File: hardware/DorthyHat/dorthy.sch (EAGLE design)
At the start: 40 parts, among them J1 90325-0004, J2 90325-0004

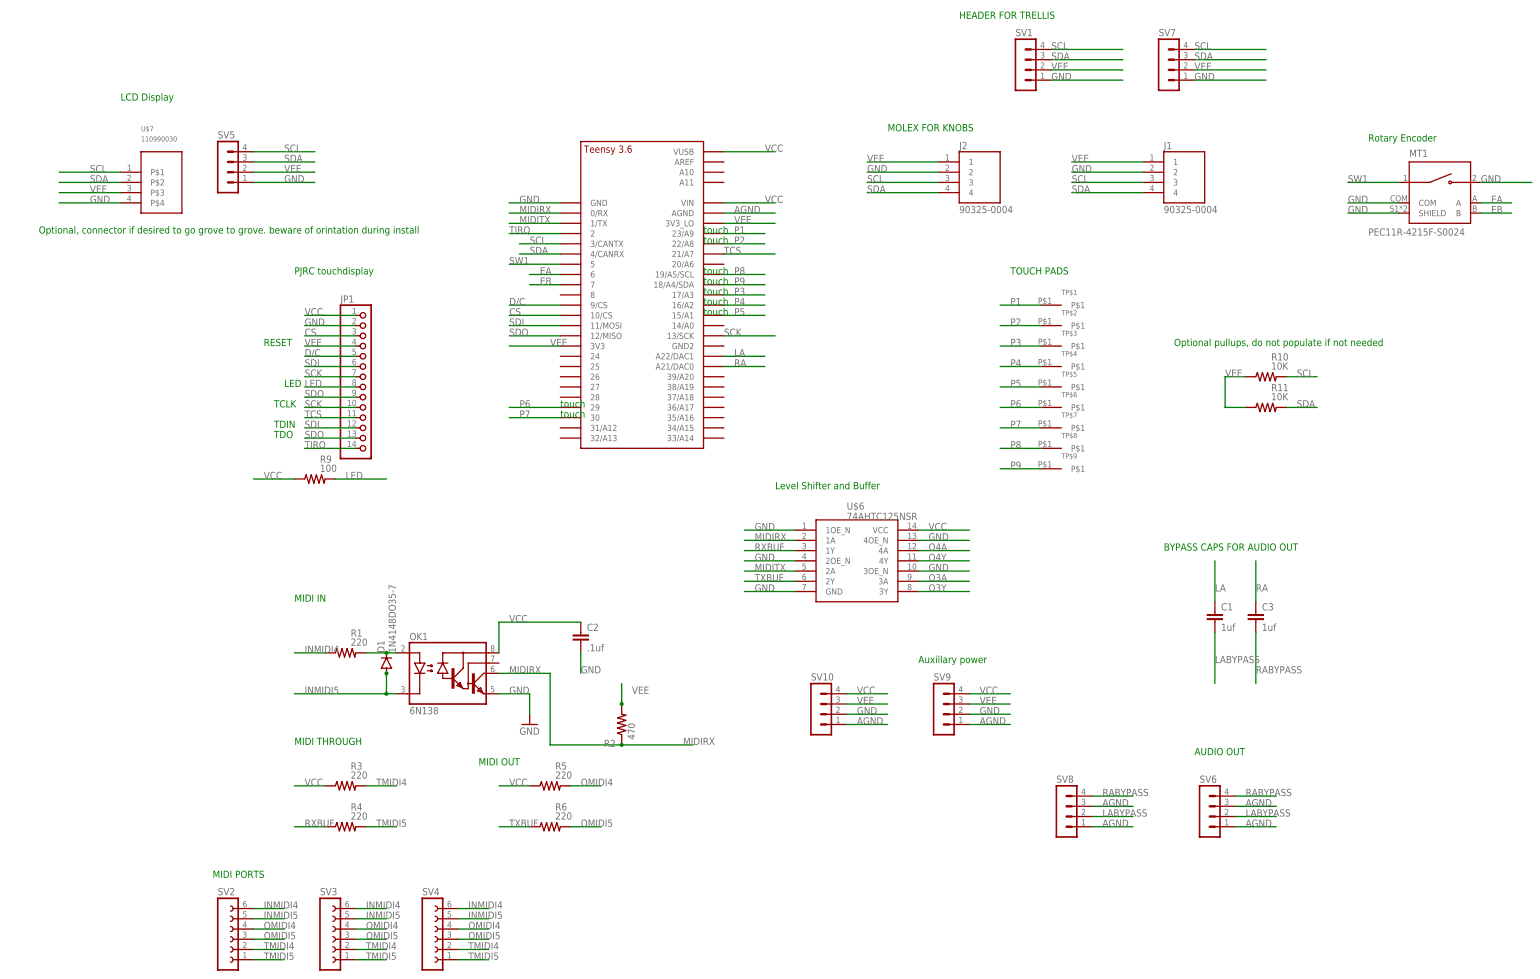
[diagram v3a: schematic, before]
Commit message: change shematic (back) to teensy 4.0, with audio sheild and touch display
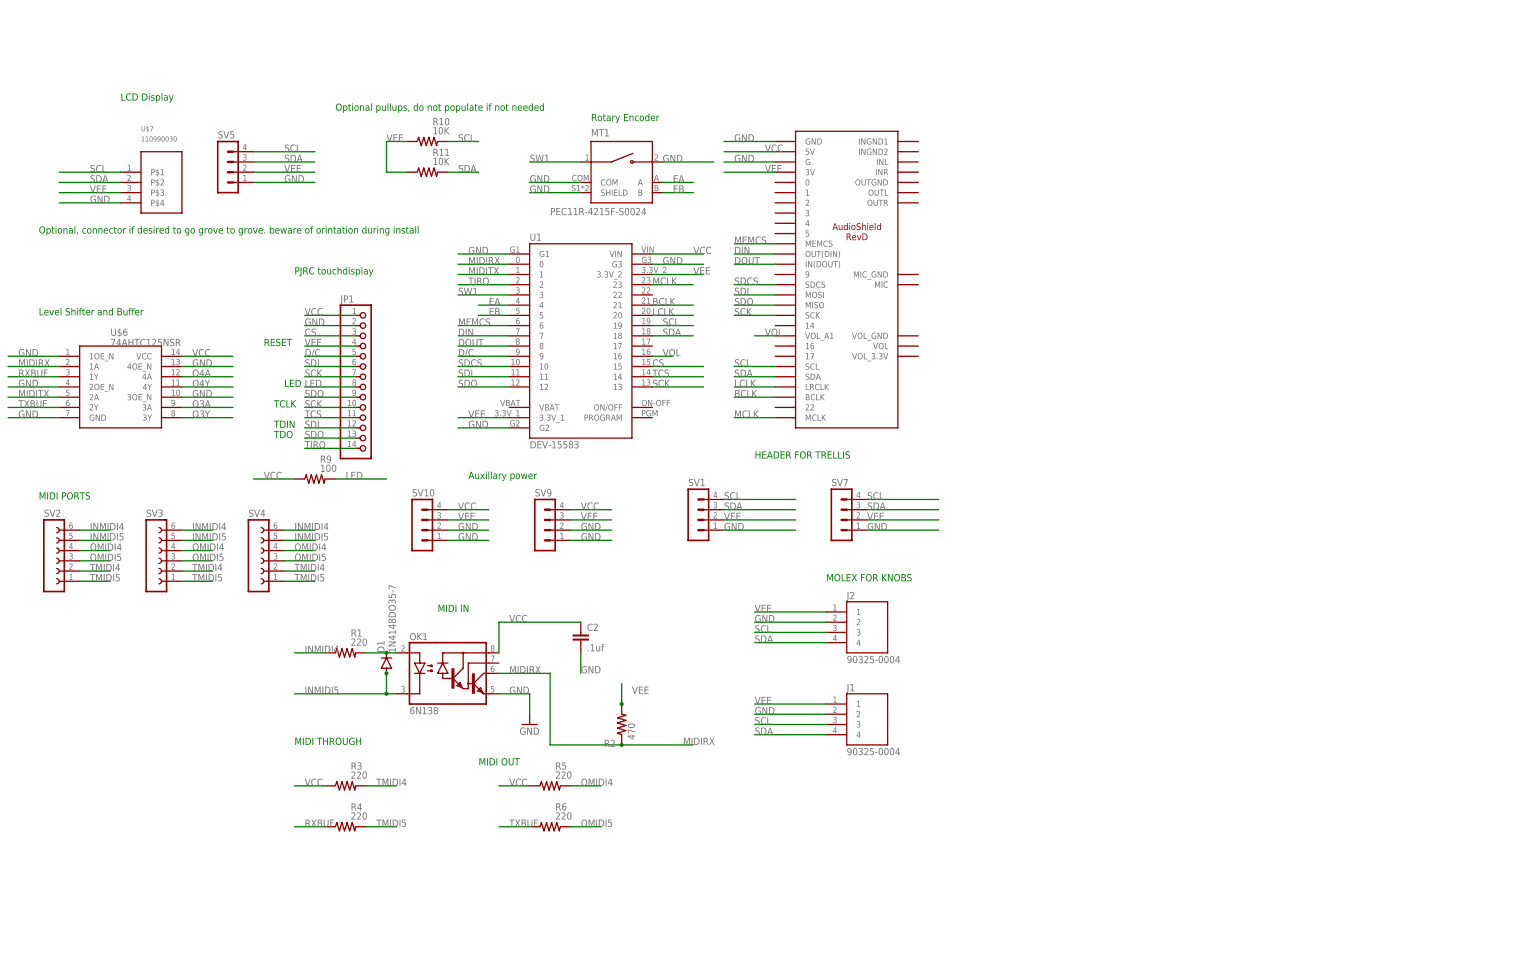
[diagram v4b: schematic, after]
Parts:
- removed C1, C3: 1uf, capacitor-wima:C5/3.5
- removed SV6, SV8: (no value), con-lstb:MA04-1
- removed TP$1, TP$2, TP$3, TP$4, TP$5, TP$6, TP$7, TP$8, TP$9: CAPACITIVE_TOUCH_PAD, CRcustom:CAPACITIVE_TOUCH_PAD
- removed U$1: TEENSY_3.5/3.6_BASIC, Teensy356:TEENSY_3.5/3.6_BASIC
- added U$2: AUDIOSHIELD-REVD, Teensy_Audioshield:AUDIOSHIELD-REVD
- added U1: DEV-15583, DEV-15583:DEV-15583
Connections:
- removed net AGND: SV10.1, SV6.1, SV6.3, SV8.1, SV8.3, SV9.1, U$1.AGND
- removed net LA: C1.1, U$1.A22/DAC1
- removed net LABYPASS: C1.2, SV6.2, SV8.2
- removed net P1: TP$1.P$1, U$1.23/A9
- removed net P2: TP$2.P$1, U$1.22/A8
- removed net P3: TP$3.P$1, U$1.17/A3
- removed net P4: TP$4.P$1, U$1.16/A2
- removed net P5: TP$5.P$1, U$1.15/A1
- removed net P6: TP$6.P$1, U$1.29
- removed net P7: TP$7.P$1, U$1.30
- removed net P8: TP$8.P$1, U$1.19/A5/SCL
- removed net P9: TP$9.P$1, U$1.18/A4/SDA
- removed net RA: C3.1, U$1.A21/DAC0
- removed net RABYPASS: C3.2, SV6.4, SV8.4
- new net BCLK: U$2.BCLK, U1.21
- new net DIN: U$2.OUT(DIN), U1.7
- new net DOUT: U$2.IN(DOUT), U1.8
- new net LCLK: U$2.LRCLK, U1.20
- new net MCLK: U$2.MCLK, U1.23
- new net MEMCS: U$2.MEMCS, U1.6
- new net SDCS: U$2.SDCS, U1.10
- new net VOL: U$2.VOL_A1, U1.16
- net CS: now also U1.15; no longer U$1.10/CS
- net D/C: now also U1.9; no longer U$1.9/CS
- net EA: now also U1.4; no longer U$1.6
- net EB: now also U1.5; no longer U$1.7
- net GND: now also SV10.1, SV9.1, U$2.G, U$2.GND, U1.G1, U1.G2, U1.G3; no longer U$1.GND
- net MIDIRX: now also U1.0; no longer U$1.0/RX
- net MIDITX: now also U1.1; no longer U$1.1/TX
- net SCK: now also U$2.SCK, U1.13; no longer U$1.13/SCK
- net SCL: now also U$2.SCL, U1.19; no longer U$1.3/CANTX
- net SDA: now also U$2.SDA, U1.18; no longer U$1.4/CANRX
- net SDI: now also U$2.MOSI, U1.11; no longer U$1.11/MOSI
- net SDO: now also U$2.MISO, U1.12; no longer U$1.12/MISO
- net SW1: now also U1.3; no longer U$1.5
- net TCS: now also U1.14; no longer U$1.21/A7
- net TIRQ: now also U1.2; no longer U$1.2
- net VCC: now also U$2.5V, U1.VIN; no longer U$1.VIN, U$1.VUSB
- net VEE: now also U$2.3V, U1.3.3V_1, U1.3.3V_2; no longer U$1.3V3, U$1.3V3_LO
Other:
- note removed: "AUDIO OUT"
- note removed: "BYPASS CAPS FOR AUDIO OUT"
- note removed: "TOUCH PADS"
- note removed: "touch"
- moved on the sheet: J1, J2, MT1, R10, R11, SV1, SV10, SV2, SV3, SV4, SV7, SV9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

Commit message: add custom footprint for the display
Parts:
- removed JP1: (no value), pinhead:PINHD-1X14
- added U$1: ILI9341, ili9341:ILI9341
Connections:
- net CS: now also U$1.CS; no longer JP1.3
- net D/C: now also U$1.DC; no longer JP1.5
- net GND: now also U$1.GND; no longer JP1.2
- net LED: now also U$1.LED; no longer JP1.8
- net SCK: now also U$1.SCK, U$1.TCLK; no longer JP1.10, JP1.7
- net SDI: now also U$1.SDI, U$1.TDIN; no longer JP1.12, JP1.6
- net SDO: now also U$1.SDO, U$1.TDO; no longer JP1.13, JP1.9
- net TCS: now also U$1.TCS; no longer JP1.11
- net TIRQ: now also U$1.TIRQ; no longer JP1.14
- net VCC: now also U$1.VCC; no longer JP1.1
- net VEE: now also U$1.RST; no longer JP1.4
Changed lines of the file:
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@@
 <part name="SV3" library="con-lsta" library_urn="urn:adsk.eagle:library:161" deviceset="FE06-1" device="" package3d_urn="urn:adsk.eagle:package:8191/1"/>
 <part name="SV4" library="con-lsta" library_urn="urn:adsk.eagle:library:161" deviceset="FE06-1" device="" package3d_urn="urn:adsk.eagle:package:8191/1"/>
-<part name="JP1" library="pinhead" library_urn="urn:adsk.eagle:library:325" deviceset="PINHD-1X14" device="" package3d_urn="urn:adsk.eagle:package:22417/2"/>
 <part name="R10" library="rcl" library_urn="urn:adsk.eagle:library:334" deviceset="R-US_" device="0207/10" package3d_urn="urn:adsk.eagle:package:23491/2" value="10K"/>
 <part name="R11" library="rcl" library_urn="urn:adsk.eagle:library:334" deviceset="R-US_" device="0207/10" package3d_urn="urn:adsk.eagle:package:23491/2" value="10K"/>
@@
 <part name="U1" library="DEV-15583" deviceset="DEV-15583" device=""/>
 <part name="U$2" library="Teensy_Audioshield" deviceset="AUDIOSHIELD-REVD" device=""/>
+<part name="U$1" library="ili9341" deviceset="ILI9341" device=""/>
 </parts>
 <sheets>
@@
 <attribute name="NAME" x="-74.93" y="92.202" size="1.778" layer="95"/>
 </instance>
-<instance part="JP1" gate="A" x="-45.72" y="127" smashed="yes">
-<attribute name="NAME" x="-52.07" y="145.415" size="1.778" layer="95"/>
-<attribute name="VALUE" x="-52.07" y="104.14" size="1.778" layer="96"/>
-</instance>
 <instance part="R10" gate="G$1" x="-30.48" y="185.42" smashed="yes">
 <attribute name="NAME" x="-29.21" y="189.4586" size="1.778" layer="95"/>
@@
 </instance>
 <instance part="U$2" gate="G$1" x="73.66" y="149.86" smashed="yes"/>
+<instance part="U$1" gate="G$1" x="-48.26" y="142.24" smashed="yes">
+<attribute name="NAME" x="-48.26" y="147.32" size="1.27" layer="95"/>
+<attribute name="VALUE" x="-48.26" y="144.78" size="1.27" layer="96"/>
+</instance>
 </instances>
 <busses>
@@
 </segment>
 <segment>
-<pinref part="JP1" gate="A" pin="1"/>
 <wire x1="-48.26" y1="142.24" x2="-60.96" y2="142.24" width="0.1524" layer="91"/>
 <label x="-60.96" y="142.24" size="1.778" layer="95"/>
+<pinref part="U$1" gate="G$1" pin="VCC"/>
 </segment>
 <segment>
@@
 </segment>
 <segment>
-<pinref part="JP1" gate="A" pin="2"/>
 <wire x1="-48.26" y1="139.7" x2="-60.96" y2="139.7" width="0.1524" layer="91"/>
 <label x="-60.96" y="139.7" size="1.778" layer="95"/>
+<pinref part="U$1" gate="G$1" pin="GND"/>
 </segment>
 <segment>
@@
 </segment>
 <segment>
-<pinref part="JP1" gate="A" pin="4"/>
 <wire x1="-48.26" y1="134.62" x2="-60.96" y2="134.62" width="0.1524" layer="91"/>
 <label x="-60.96" y="134.62" size="1.778" layer="95"/>
+<pinref part="U$1" gate="G$1" pin="RST"/>
 </segment>
 <segment>
@@
 <net name="CS" class="0">
 <segment>
-<pinref part="JP1" gate="A" pin="3"/>
 <wire x1="-48.26" y1="137.16" x2="-60.96" y2="137.16" width="0.1524" layer="91"/>
 <label x="-60.96" y="137.16" size="1.778" layer="95"/>
+<pinref part="U$1" gate="G$1" pin="CS"/>
 </segment>
 <segment>
@@
 <net name="D/C" class="0">
 <segment>
-<pinref part="JP1" gate="A" pin="5"/>
 <wire x1="-48.26" y1="132.08" x2="-60.96" y2="132.08" width="0.1524" layer="91"/>
 <label x="-60.96" y="132.08" size="1.778" layer="95"/>
+<pinref part="U$1" gate="G$1" pin="DC"/>
 </segment>
 <segment>
@@
 <net name="SDI" class="0">
 <segment>
-<pinref part="JP1" gate="A" pin="6"/>
 <wire x1="-48.26" y1="129.54" x2="-60.96" y2="129.54" width="0.1524" layer="91"/>
 <label x="-60.96" y="129.54" size="1.778" layer="95"/>
-</segment>
-<segment>
-<pinref part="JP1" gate="A" pin="12"/>
-<wire x1="-48.26" y1="114.3" x2="-60.96" y2="114.3" width="0.1524" layer="91"/>
-<label x="-60.96" y="114.3" size="1.778" layer="95"/>
+<pinref part="U$1" gate="G$1" pin="SDI"/>
 </segment>
 <segment>
@@
 <label x="45.72" y="147.32" size="1.778" layer="95"/>
 </segment>
+<segment>
+<wire x1="-48.26" y1="114.3" x2="-60.96" y2="114.3" width="0.1524" layer="91"/>
+<label x="-60.96" y="114.3" size="1.778" layer="95"/>
+<pinref part="U$1" gate="G$1" pin="TDIN"/>
+</segment>
 </net>
 <net name="SCK" class="0">
 <segment>
-<pinref part="JP1" gate="A" pin="7"/>
 <wire x1="-48.26" y1="127" x2="-60.96" y2="127" width="0.1524" layer="91"/>
 <label x="-60.96" y="127" size="1.778" layer="95"/>
-</segment>
-<segment>
-<pinref part="JP1" gate="A" pin="10"/>
-<wire x1="-48.26" y1="119.38" x2="-60.96" y2="119.38" width="0.1524" layer="91"/>
-<label x="-60.96" y="119.38" size="1.778" layer="95"/>
+<pinref part="U$1" gate="G$1" pin="SCK"/>
 </segment>
 <segment>
@@
 <label x="45.72" y="142.24" size="1.778" layer="95"/>
 </segment>
+<segment>
+<wire x1="-48.26" y1="119.38" x2="-60.96" y2="119.38" width="0.1524" layer="91"/>
+<label x="-60.96" y="119.38" size="1.778" layer="95"/>
+<pinref part="U$1" gate="G$1" pin="TCLK"/>
+</segment>
 </net>
 <net name="SDO" class="0">
 <segment>
-<pinref part="JP1" gate="A" pin="9"/>
 <wire x1="-48.26" y1="121.92" x2="-60.96" y2="121.92" width="0.1524" layer="91"/>
 <label x="-60.96" y="121.92" size="1.778" layer="95"/>
-</segment>
-<segment>
-<pinref part="JP1" gate="A" pin="13"/>
-<wire x1="-48.26" y1="111.76" x2="-60.96" y2="111.76" width="0.1524" layer="91"/>
-<label x="-60.96" y="111.76" size="1.778" layer="95"/>
+<pinref part="U$1" gate="G$1" pin="SDO"/>
 </segment>
 <segment>
@@
 <label x="45.72" y="144.78" size="1.778" layer="95"/>
 </segment>
+<segment>
+<wire x1="-48.26" y1="111.76" x2="-60.96" y2="111.76" width="0.1524" layer="91"/>
+<label x="-60.96" y="111.76" size="1.778" layer="95"/>
+<pinref part="U$1" gate="G$1" pin="TDO"/>
+</segment>
 </net>
 <net name="TCS" class="0">
@@
 <wire x1="-48.26" y1="116.84" x2="-60.96" y2="116.84" width="0.1524" layer="91"/>
 <label x="-60.96" y="116.84" size="1.778" layer="95"/>
-<pinref part="JP1" gate="A" pin="11"/>
+<pinref part="U$1" gate="G$1" pin="TCS"/>
 </segment>
 <segment>
@@
 <net name="TIRQ" class="0">
 <segment>
-<pinref part="JP1" gate="A" pin="14"/>
 <wire x1="-48.26" y1="109.22" x2="-60.96" y2="109.22" width="0.1524" layer="91"/>
 <label x="-60.96" y="109.22" size="1.778" layer="95"/>
+<pinref part="U$1" gate="G$1" pin="TIRQ"/>
 </segment>
 <segment>
@@
 <net name="LED" class="0">
 <segment>
-<pinref part="JP1" gate="A" pin="8"/>
 <wire x1="-48.26" y1="124.46" x2="-60.96" y2="124.46" width="0.1524" layer="91"/>
 <label x="-60.96" y="124.46" size="1.778" layer="95"/>
-</segment>
-<segment>
+<pinref part="U$1" gate="G$1" pin="LED"/>
+</segment>
+<segment>
